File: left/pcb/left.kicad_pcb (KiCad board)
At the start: 2 copper layers, 100 x 75 mm, 23 parts, among them J1 Jack, U1 Hall_Sensor, U10 Hall_Sensor, U11 Hall_Sensor, U2 Hall_Sensor, U3 Hall_Sensor, U4 Hall_Sensor, U5 Hall_Sensor, U6 Hall_Sensor, U7 74HC4051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

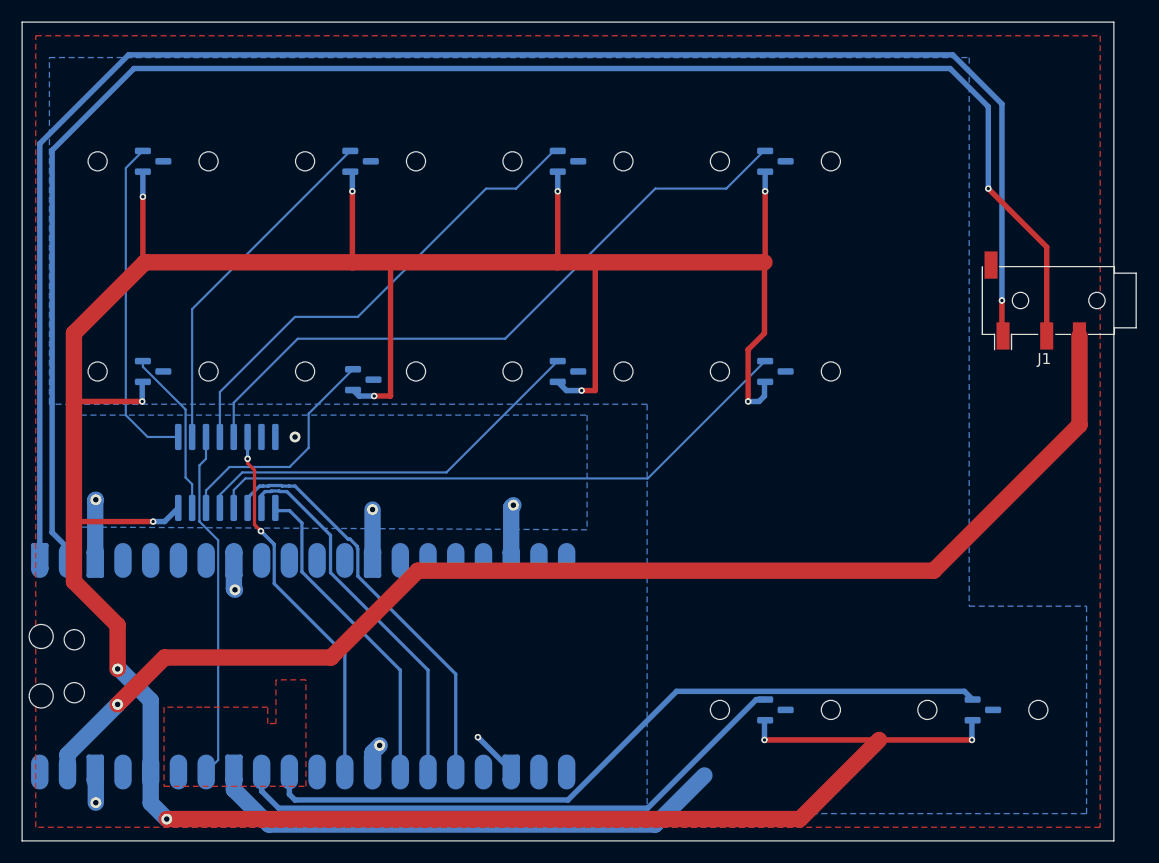
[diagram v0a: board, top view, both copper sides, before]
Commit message: add holes to fill and some rerouting
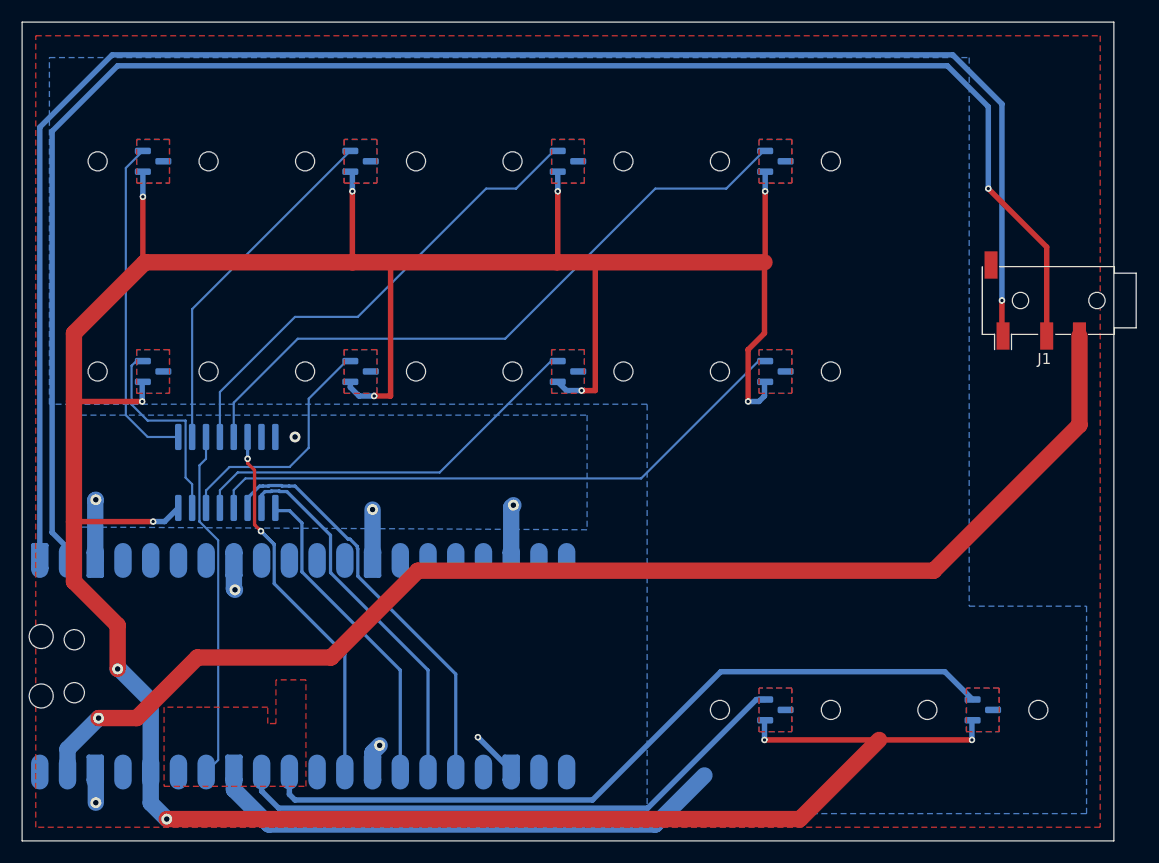
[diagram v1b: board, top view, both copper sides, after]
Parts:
- moved U2 0.79 mm to (131.0, 87.0)
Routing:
- net /KEY2: track 15.3 -> 18.6 mm
- net /KEY0: track 69.3 -> 70.8 mm
- net /UART-RX: track 152.5 -> 153.7 mm
- net /UART-TX: track 152.8 -> 153.7 mm
- net /KEY3: track 21.5 -> 22.4 mm
- net +3V3: track 304.1 -> 304.9 mm
